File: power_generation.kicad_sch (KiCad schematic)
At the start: 35 parts, among them J301 61300211121, J302 61300211121, J303 EMI shield frame, U301 AP64500SP-13, U302 AP64500SP-13

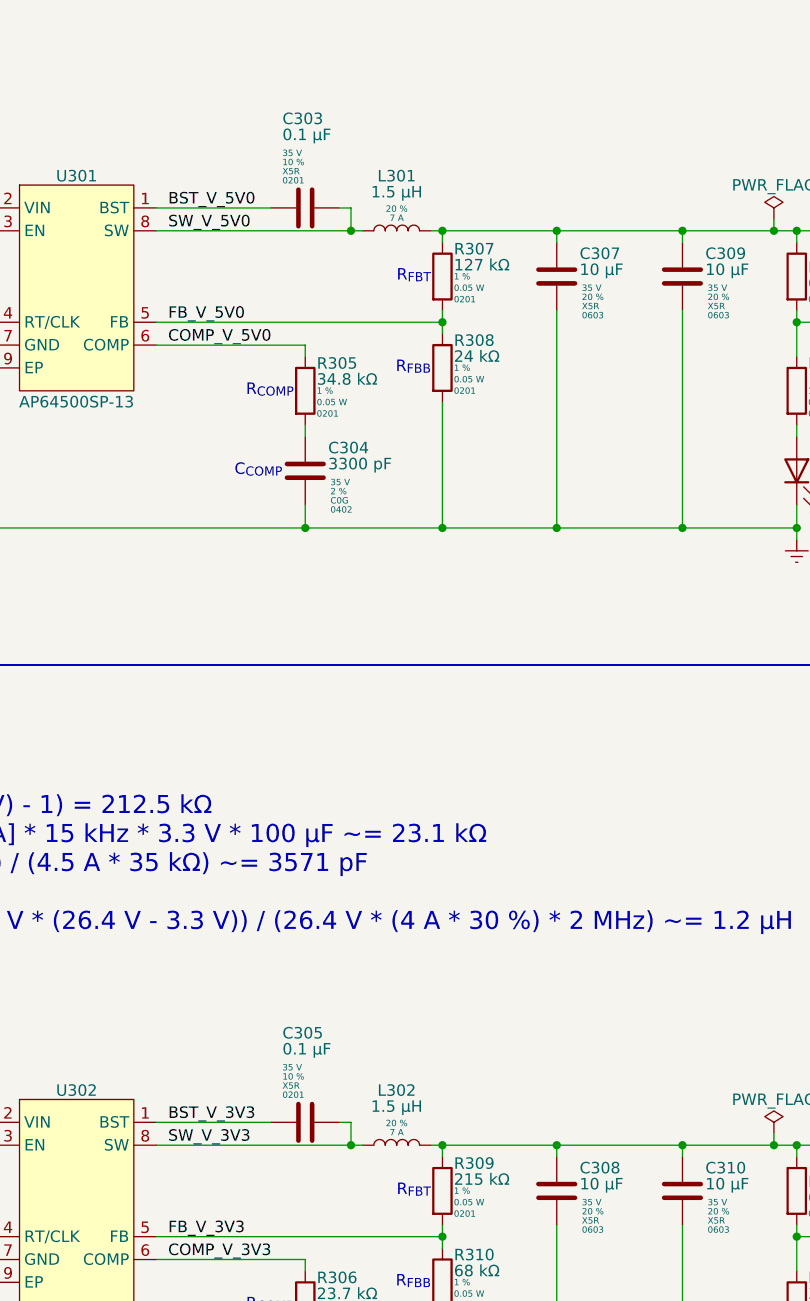
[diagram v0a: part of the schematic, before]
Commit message: Fix symbols and footprint assignments
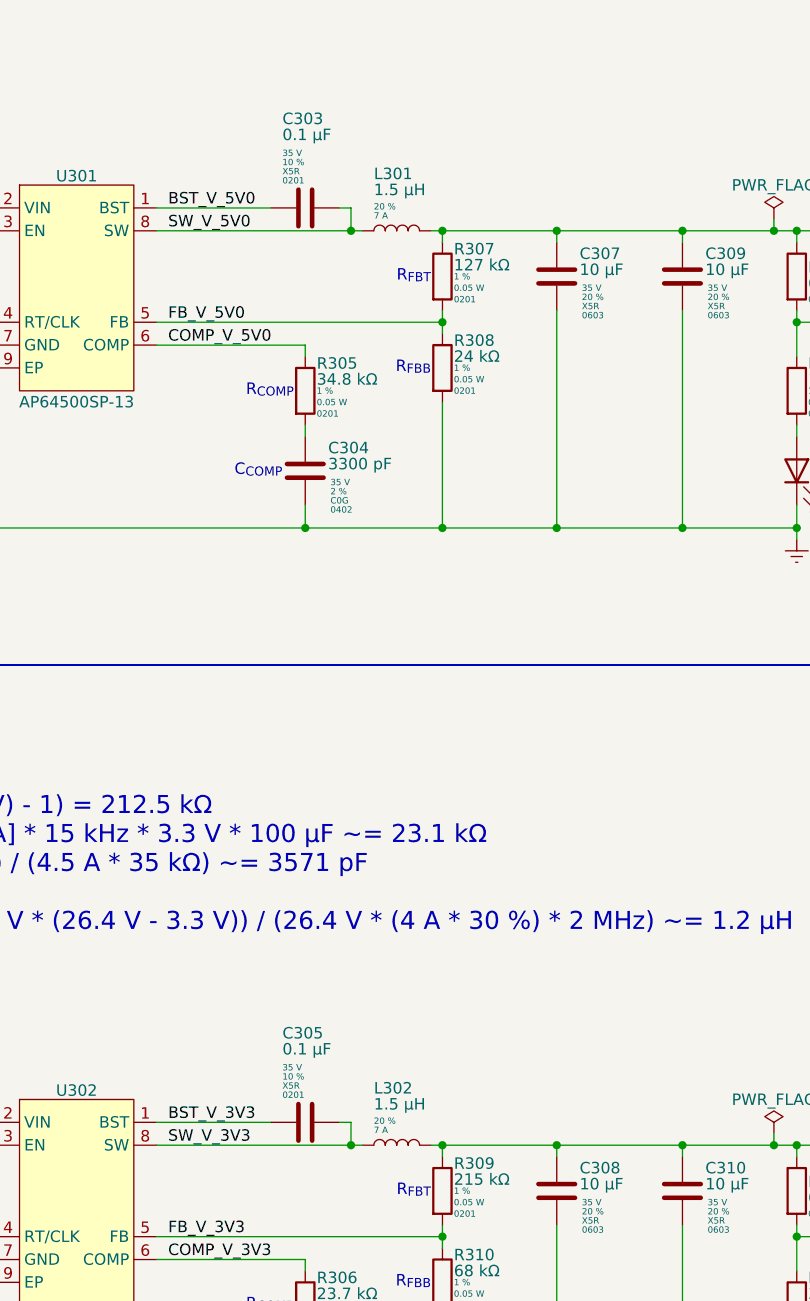
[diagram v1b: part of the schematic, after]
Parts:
- J301, J302: footprint Connector_PinHeader_2.54mm:PinHeader_2x01_P2.54mm_Vertical -> Connector_PinHeader_2.54mm:PinHeader_1x02_P2.54mm_Vertical
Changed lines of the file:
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@@
 			)
 		)
-		(property "Footprint" "Connector_PinHeader_2.54mm:PinHeader_2x01_P2.54mm_Vertical"
+		(property "Footprint" "Connector_PinHeader_2.54mm:PinHeader_1x02_P2.54mm_Vertical"
 			(at 195.58 102.87 0)
 			(effects
@@
 		(dnp no)
 		(property "Reference" "L302"
-			(at 137.16 194.056 90)
+			(at 134.62 193.802 90)
 			(effects
 				(font
 					(size 1.27 1.27)
 				)
-				(justify top)
+				(justify right top)
 			)
 		)
 		(property "Value" "1.5 µH"
-			(at 137.16 195.834 90)
+			(at 134.62 195.58 90)
 			(effects
 				(font
 					(size 1.27 1.27)
 				)
-				(justify top)
+				(justify right top)
 			)
 		)
@@
 		)
 		(property "Current rating" "7 A"
-			(at 137.16 198.374 90)
+			(at 134.62 198.12 90)
 			(effects
 				(font
 					(size 0.7 0.7)
 				)
-				(justify top)
+				(justify right top)
 			)
 		)
 		(property "Tolerance" "20 %"
-			(at 137.16 197.358 90)
+			(at 134.62 197.104 90)
 			(effects
 				(font
 					(size 0.7 0.7)
 				)
-				(justify top)
+				(justify right top)
 			)
 		)
@@
 	)
 	(symbol
+		(lib_name "R_1")
 		(lib_id "Device:R")
 		(at 181.61 102.87 0)
@@
 			)
 		)
-		(property "Footprint" "Connector_PinHeader_2.54mm:PinHeader_2x01_P2.54mm_Vertical"
+		(property "Footprint" "Connector_PinHeader_2.54mm:PinHeader_1x02_P2.54mm_Vertical"
 			(at 195.58 204.47 0)
 			(effects
@@
 	)
 	(symbol
+		(lib_name "C_1")
 		(lib_id "Device:C")
 		(at 127 95.25 90)
@@
 	)
 	(symbol
+		(lib_name "L_1")
 		(lib_id "Device:L")
 		(at 137.16 97.79 90)
@@
 		(dnp no)
 		(property "Reference" "L301"
-			(at 137.16 92.456 90)
+			(at 134.62 92.202 90)
 			(effects
 				(font
 					(size 1.27 1.27)
 				)
-				(justify top)
+				(justify right top)
 			)
 		)
 		(property "Value" "1.5 µH"
-			(at 137.16 94.234 90)
+			(at 134.62 93.98 90)
 			(effects
 				(font
 					(size 1.27 1.27)
 				)
-				(justify top)
+				(justify right top)
 			)
 		)
@@
 		)
 		(property "Current rating" "7 A"
-			(at 137.16 96.774 90)
+			(at 134.62 96.52 90)
 			(effects
 				(font
 					(size 0.7 0.7)
 				)
-				(justify top)
+				(justify right top)
 			)
 		)
 		(property "Tolerance" "20 %"
-			(at 137.16 95.758 90)
+			(at 134.62 95.504 90)
 			(effects
 				(font
 					(size 0.7 0.7)
 				)
-				(justify top)
+				(justify right top)
 			)
 		)

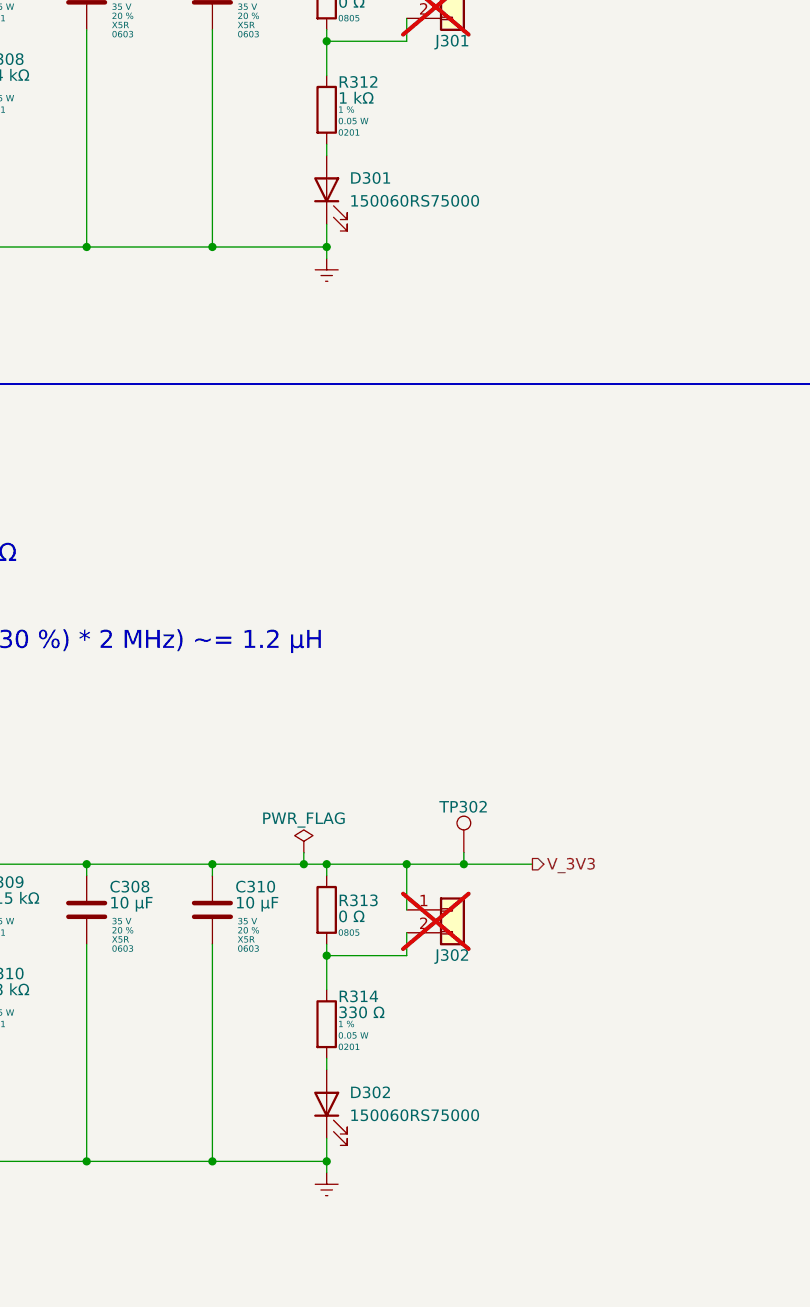
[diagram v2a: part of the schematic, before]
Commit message: Rework Red LED BOM and info, rework debug USB-to-UART
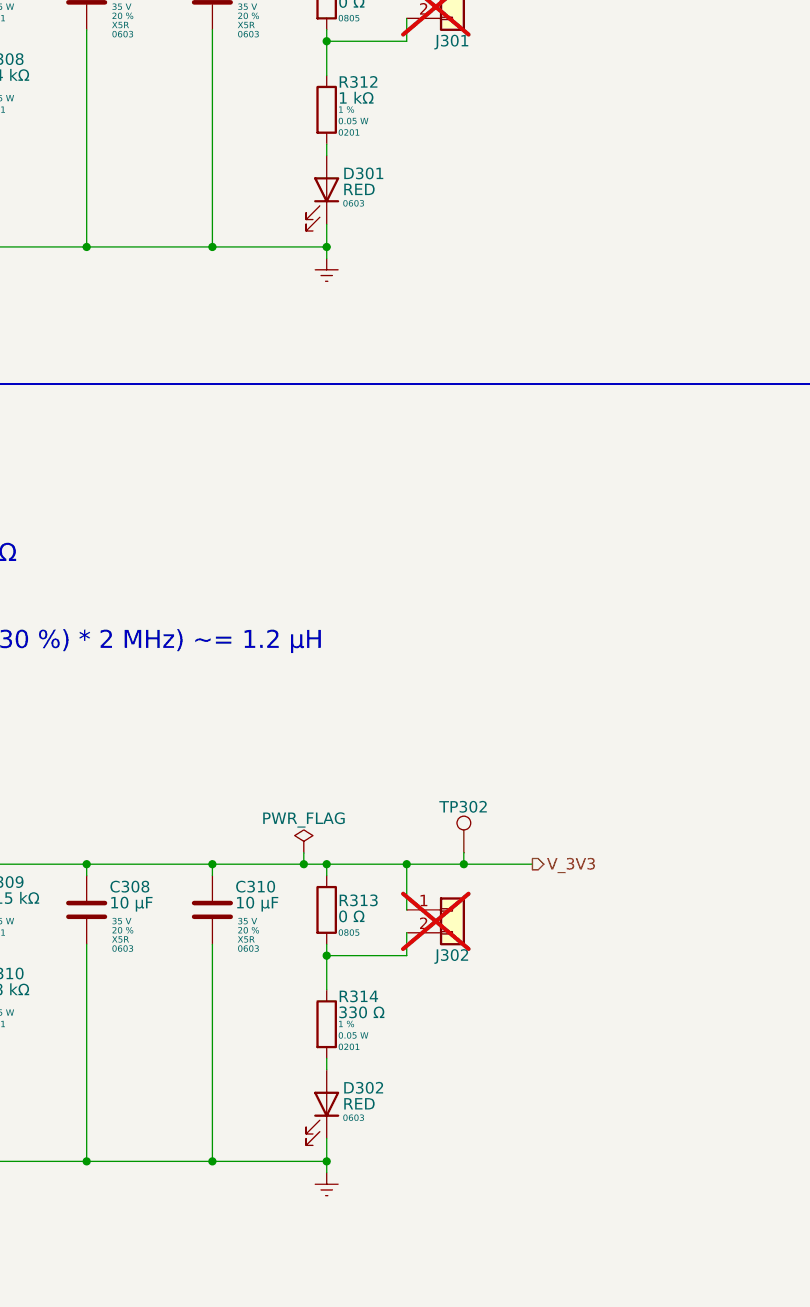
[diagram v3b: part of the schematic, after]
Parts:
- D301, D302: value 150060RS75000 -> RED; Size (none) -> 0603
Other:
- moved on the sheet: D301
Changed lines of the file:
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@@
 			)
 		)
-		(property "Datasheet" "~"
+		(property "Datasheet" "https://www.laird.com/document/datasheet/bmi-s-202-sales"
 			(at 355.6 148.59 0)
 			(effects
@@
 	)
 	(symbol
+		(lib_id "Device:LED")
+		(at 181.61 226.06 270)
+		(mirror x)
+		(unit 1)
+		(exclude_from_sim no)
+		(in_bom yes)
+		(on_board yes)
+		(dnp no)
+		(property "Reference" "D302"
+			(at 183.388 224.282 90)
+			(effects
+				(font
+					(size 1.27 1.27)
+				)
+				(justify left)
+			)
+		)
+		(property "Value" "RED"
+			(at 183.388 226.06 90)
+			(effects
+				(font
+					(size 1.27 1.27)
+				)
+				(justify left)
+			)
+		)
+		(property "Footprint" "LED_SMD:LED_0603_1608Metric"
+			(at 181.61 226.06 0)
+			(effects
+				(font
+					(size 1.27 1.27)
+				)
+				(hide yes)
+			)
+		)
+		(property "Datasheet" "https://www.we-online.com/components/products/datasheet/150060RS75000.pdf"
+			(at 181.61 226.06 0)
+			(effects
+				(font
+					(size 1.27 1.27)
+				)
+				(hide yes)
+			)
+		)
+		(property "Description" "Red 625nm LED Indication - Discrete 2V 0603 (1608 Metric)"
+			(at 181.61 226.06 0)
+			(effects
+				(font
+					(size 1.27 1.27)
+				)
+				(hide yes)
+			)
+		)
+		(property "MPN" "150060RS75000"
+			(at 181.61 226.06 0)
+			(effects
+				(font
+					(size 1.27 1.27)
+				)
+				(hide yes)
+			)
+		)
+		(property "Manufacturer" "Würth Elektronik"
+			(at 181.61 226.06 0)
+			(effects
+				(font
+					(size 1.27 1.27)
+				)
+				(hide yes)
+			)
+		)
+		(property "Digi-Key Part Number" "732-4978-1-ND"
+			(at 181.61 226.06 90)
+			(effects
+				(font
+					(size 1.27 1.27)
+				)
+				(hide yes)
+			)
+		)
+		(property "Size" "0603"
+			(at 183.388 227.584 90)
+			(effects
+				(font
+					(size 0.7 0.7)
+				)
+				(justify left)
+			)
+		)
+		(pin "2"
+		)
+		(pin "1"
+		)
+		(instances
+			(project "linux-sbc"
+				(path "/fa11a02f-8043-4153-ab69-88d766503017/707b7ecb-79e2-4dd5-ae9a-df7ce3b9c75b"
+					(reference "D302")
+					(unit 1)
+				)
+			)
+		)
+	)
+	(symbol
 		(lib_id "Connector_Generic:Conn_01x02")
 		(at 195.58 204.47 0)
@@
 	(symbol
 		(lib_id "Device:LED")
-		(at 181.61 124.46 90)
+		(at 181.61 124.46 270)
+		(mirror x)
 		(unit 1)
 		(exclude_from_sim no)
@@
 		(dnp no)
 		(property "Reference" "D301"
-			(at 184.15 123.19 90)
+			(at 183.388 122.682 90)
 			(effects
 				(font
 					(size 1.27 1.27)
 				)
-				(justify right)
+				(justify left)
 			)
 		)
-		(property "Value" "150060RS75000"
-			(at 184.15 125.73 90)
+		(property "Value" "RED"
+			(at 183.388 124.46 90)
 			(effects
 				(font
 					(size 1.27 1.27)
 				)
-				(justify right)
+				(justify left)
 			)
 		)
@@
 			)
 		)
+		(property "Size" "0603"
+			(at 183.388 125.984 90)
+			(effects
+				(font
+					(size 0.7 0.7)
+				)
+				(justify left)
+			)
+		)
 		(pin "2"
 		)
@@
 					(unit 1)
 				)
-			)
-		)
-	)
-	(symbol
-		(lib_id "Device:LED")
-		(at 181.61 226.06 90)
-		(unit 1)
-		(exclude_from_sim no)
-		(in_bom yes)
-		(on_board yes)
-		(dnp no)
-		(property "Reference" "D302"
-			(at 184.15 224.79 90)
-			(effects
-				(font
-					(size 1.27 1.27)
-				)
-				(justify right)
-			)
-		)
-		(property "Value" "150060RS75000"
-			(at 184.15 227.33 90)
-			(effects
-				(font
-					(size 1.27 1.27)
-				)
-				(justify right)
-			)
-		)
-		(property "Footprint" "LED_SMD:LED_0603_1608Metric"
-			(at 181.61 226.06 0)
-			(effects
-				(font
-					(size 1.27 1.27)
-				)
-				(hide yes)
-			)
-		)
-		(property "Datasheet" "https://www.we-online.com/components/products/datasheet/150060RS75000.pdf"
-			(at 181.61 226.06 0)
-			(effects
-				(font
-					(size 1.27 1.27)
-				)
-				(hide yes)
-			)
-		)
-		(property "Description" "Red 625nm LED Indication - Discrete 2V 0603 (1608 Metric)"
-			(at 181.61 226.06 0)
-			(effects
-				(font
-					(size 1.27 1.27)
-				)
-				(hide yes)
-			)
-		)
-		(property "MPN" "150060RS75000"
-			(at 181.61 226.06 0)
-			(effects
-				(font
-					(size 1.27 1.27)
-				)
-				(hide yes)
-			)
-		)
-		(property "Manufacturer" "Würth Elektronik"
-			(at 181.61 226.06 0)
-			(effects
-				(font
-					(size 1.27 1.27)
-				)
-				(hide yes)
-			)
-		)
-		(property "Digi-Key Part Number" "732-4978-1-ND"
-			(at 181.61 226.06 90)
-			(effects
-				(font
-					(size 1.27 1.27)
-				)
-				(hide yes)
-			)
-		)
-		(pin "2"
-		)
-		(pin "1"
-		)
-		(instances
-			(project "linux-sbc"
-				(path "/fa11a02f-8043-4153-ab69-88d766503017/707b7ecb-79e2-4dd5-ae9a-df7ce3b9c75b"
-					(reference "D302")
-					(unit 1)
-				)

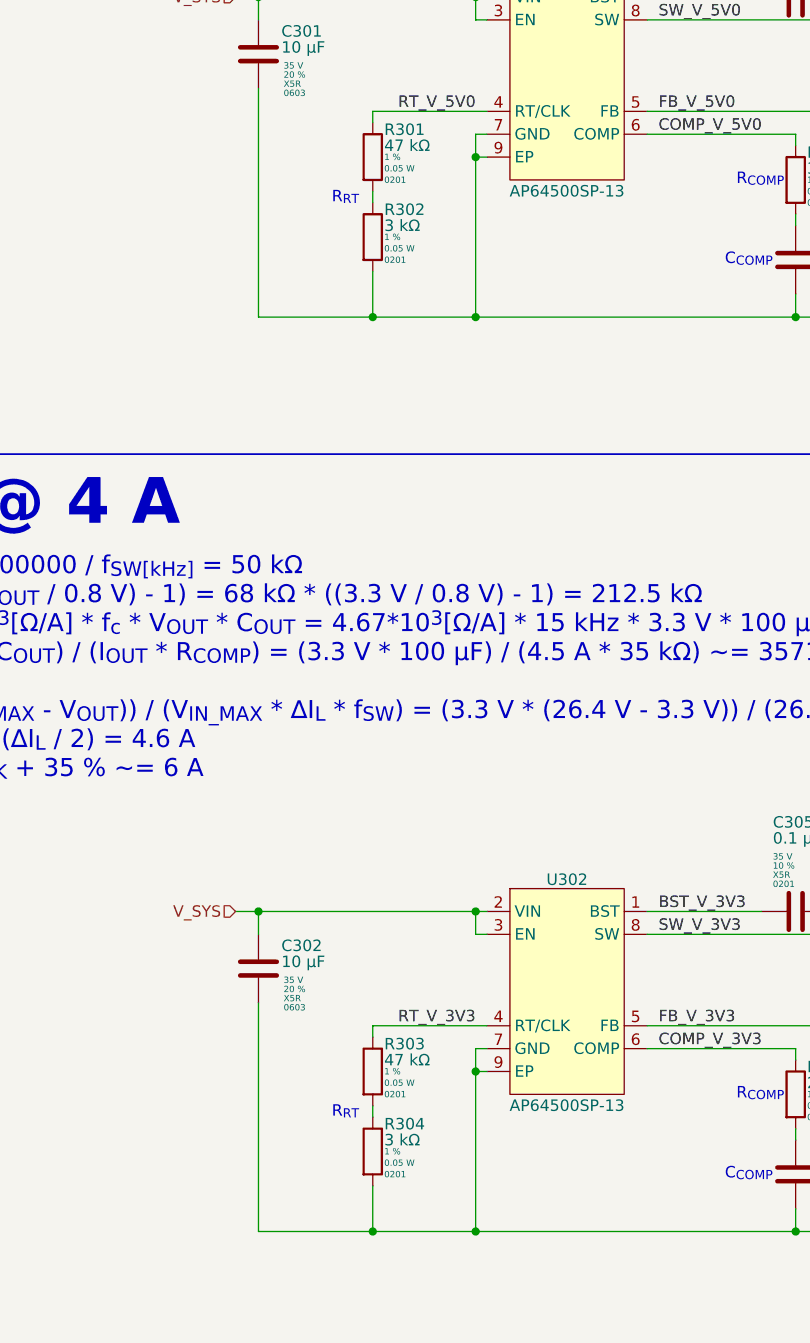
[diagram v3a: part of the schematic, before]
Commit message: Refactor BOM
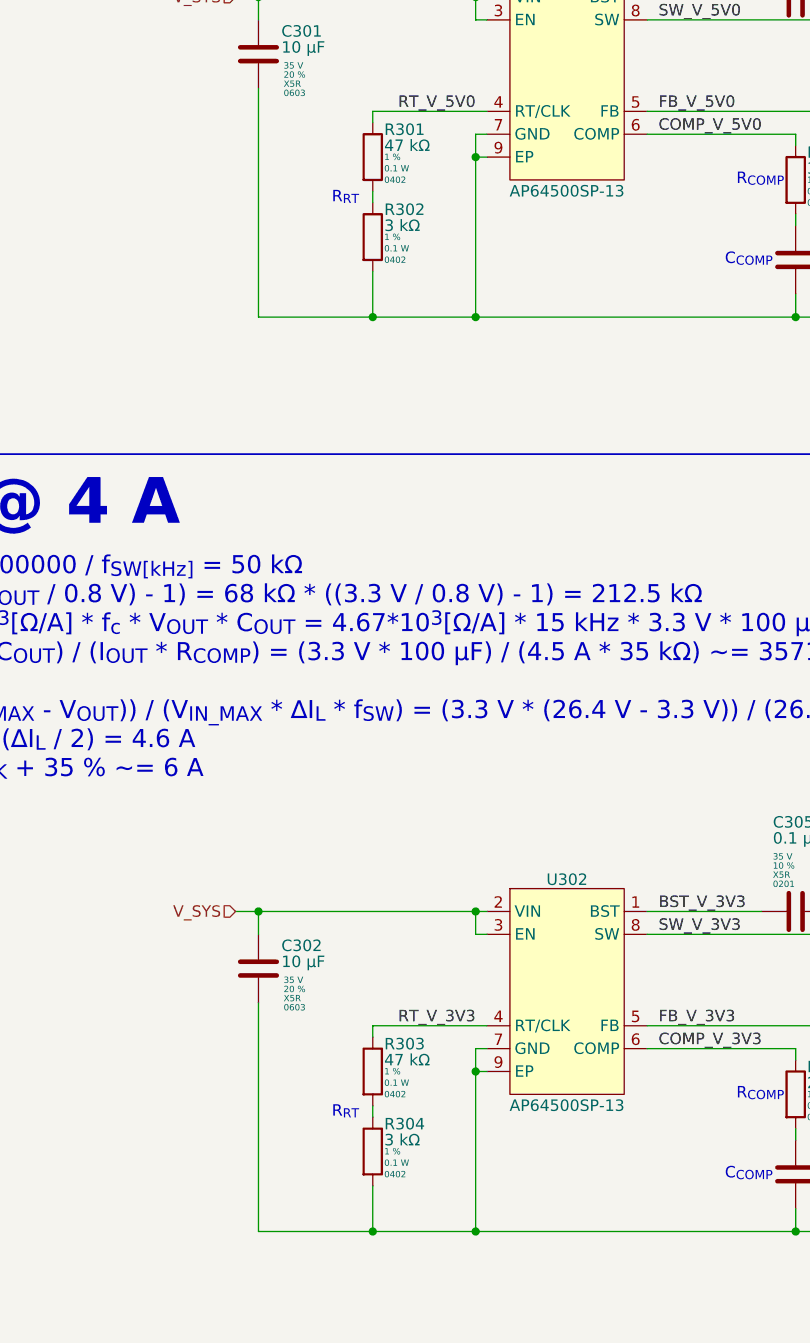
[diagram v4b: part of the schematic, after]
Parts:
- R301, R303: footprint perfect_footprints:R_0201_0603Metric -> perfect_footprints:R_0402_1005Metric; Digi-Key Part Number P123032CT-ND -> P47.0KLCT-ND; MPN ERJ-1GNF4702C -> ERJ-2RKF4702X; Power rating 0.05 W -> 0.1 W; Size 0201 -> 0402
- R302, R304: footprint perfect_footprints:R_0201_0603Metric -> perfect_footprints:R_0402_1005Metric; Digi-Key Part Number P122912CT-ND -> 738-RNCF0402DTE3K00CT-ND; MPN ERJ-1GNF3001C -> RNCF0402DTE3K00; Power rating 0.05 W -> 0.1 W; Size 0201 -> 0402
